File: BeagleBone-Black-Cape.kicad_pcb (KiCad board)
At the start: 4 copper layers, 61.9 x 92.1 mm, 77 parts, among them J501 Conn_ARM_JTAG_SWD_10, J502 3.3V, P101 BeagleBone_Black_Header, P102 BeagleBone_Black_Header, U401 LM3671, U601 cc1352p, U602 MX25R8035FZUIL0, Y601 32.768kHz, Y602 48MHz

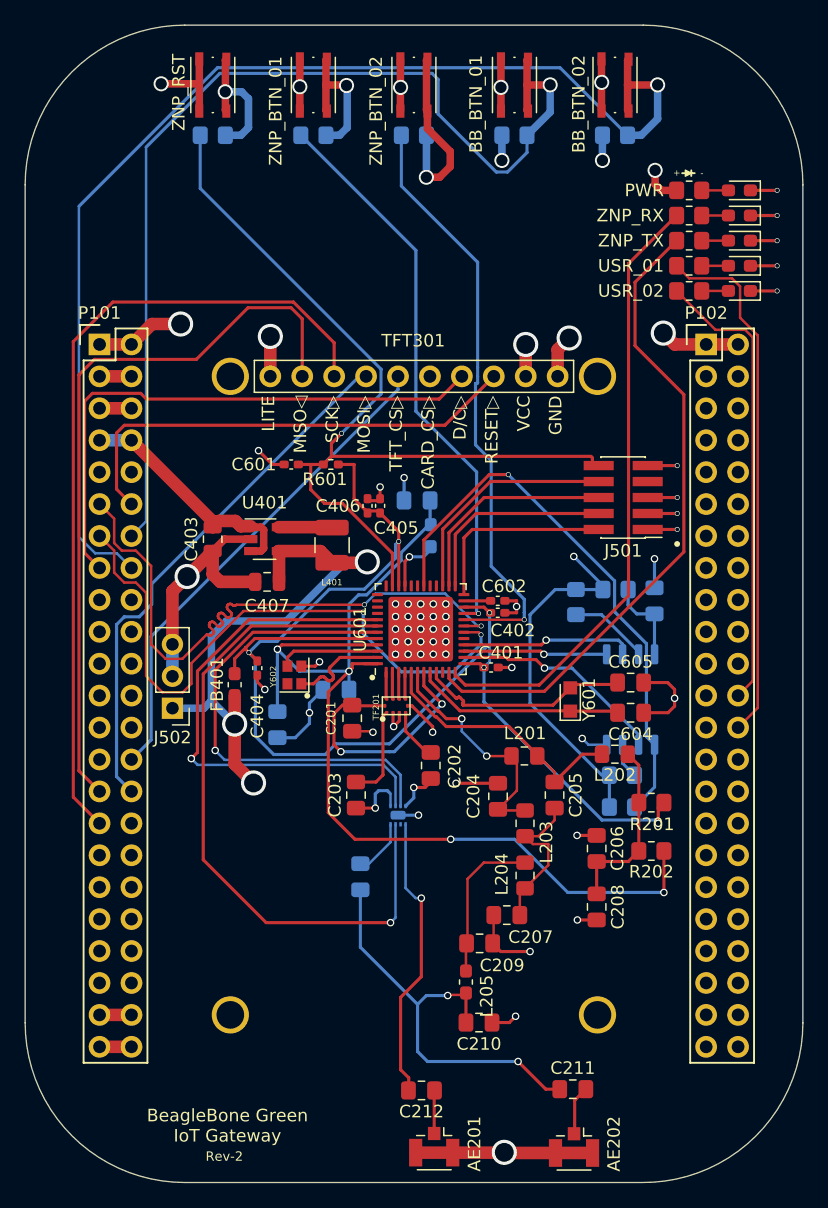
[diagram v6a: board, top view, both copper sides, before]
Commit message: lib update so it only includes user-made library
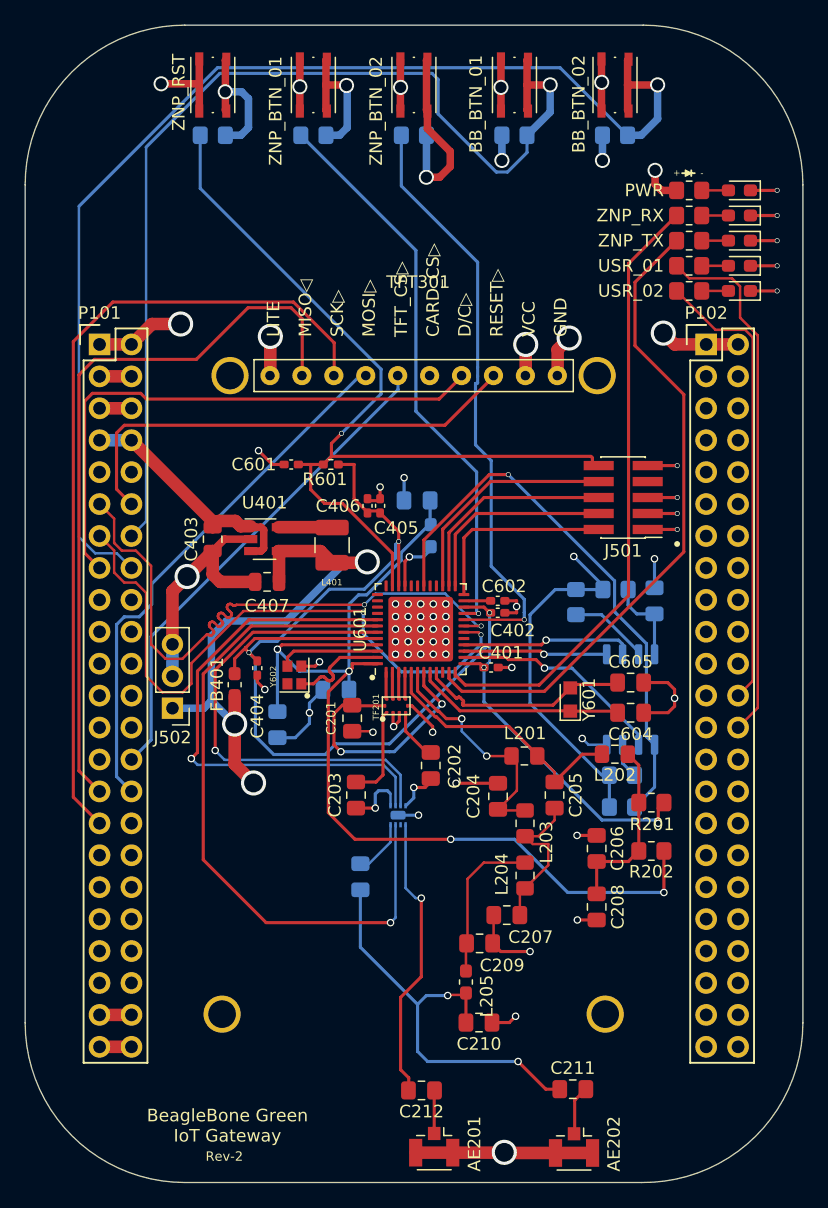
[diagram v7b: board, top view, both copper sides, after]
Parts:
- P101, P102: footprint Socket_BeagleBone_Black:Socket_BeagleBone_Black -> UserMade-BB-Zigbee-Gateway-CAPE:Socket_BeagleBone_Black
- TF201: footprint footprints:IPC_1352P -> UserMade-BB-Zigbee-Gateway-CAPE:IPC_1352P
- TF202: footprint ul_SKY13317373LF:SKY13317-373LF-BH -> UserMade-BB-Zigbee-Gateway-CAPE:SKY13317-373LF-BH
- TFT301: footprint pwr_Beaglebone:ST7735 -> UserMade-BB-Zigbee-Gateway-CAPE:ST7735
- moved TFT301 33.2 mm to (159.1, 62.3)
